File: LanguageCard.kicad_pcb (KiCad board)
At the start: 2 copper layers, 100 x 77.5 mm, 31 parts, among them J1 Apple II Expansion Bus, U1 74LS86, U10 74LS06, U2 74LS08, U3 74LS175, U4 74LS32, U5 74LS08, U6 74LS08, U7 ROM F8 (2716), U8 6264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

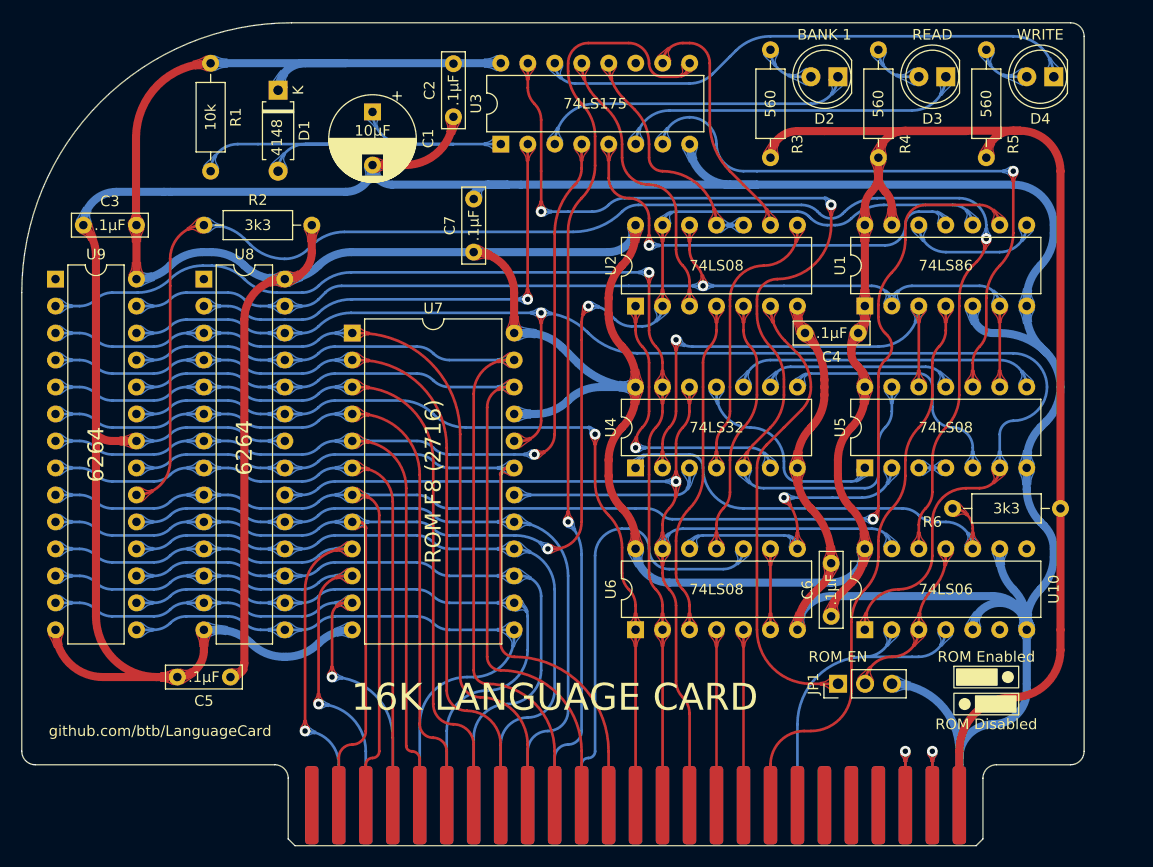
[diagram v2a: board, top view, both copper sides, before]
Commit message: update to Kicad 7
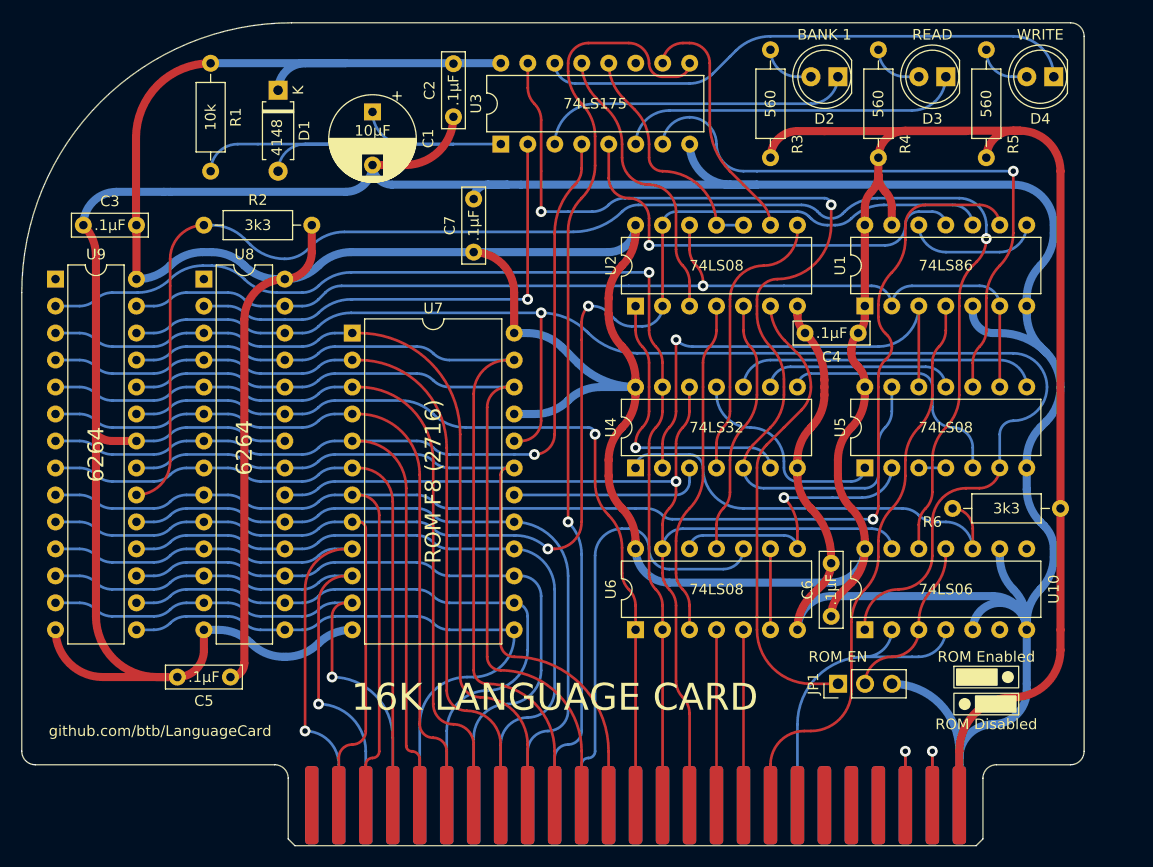
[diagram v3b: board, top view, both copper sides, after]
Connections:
- net /~{R/W} renamed /~{R}/W

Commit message: Larger ROM, enable switch
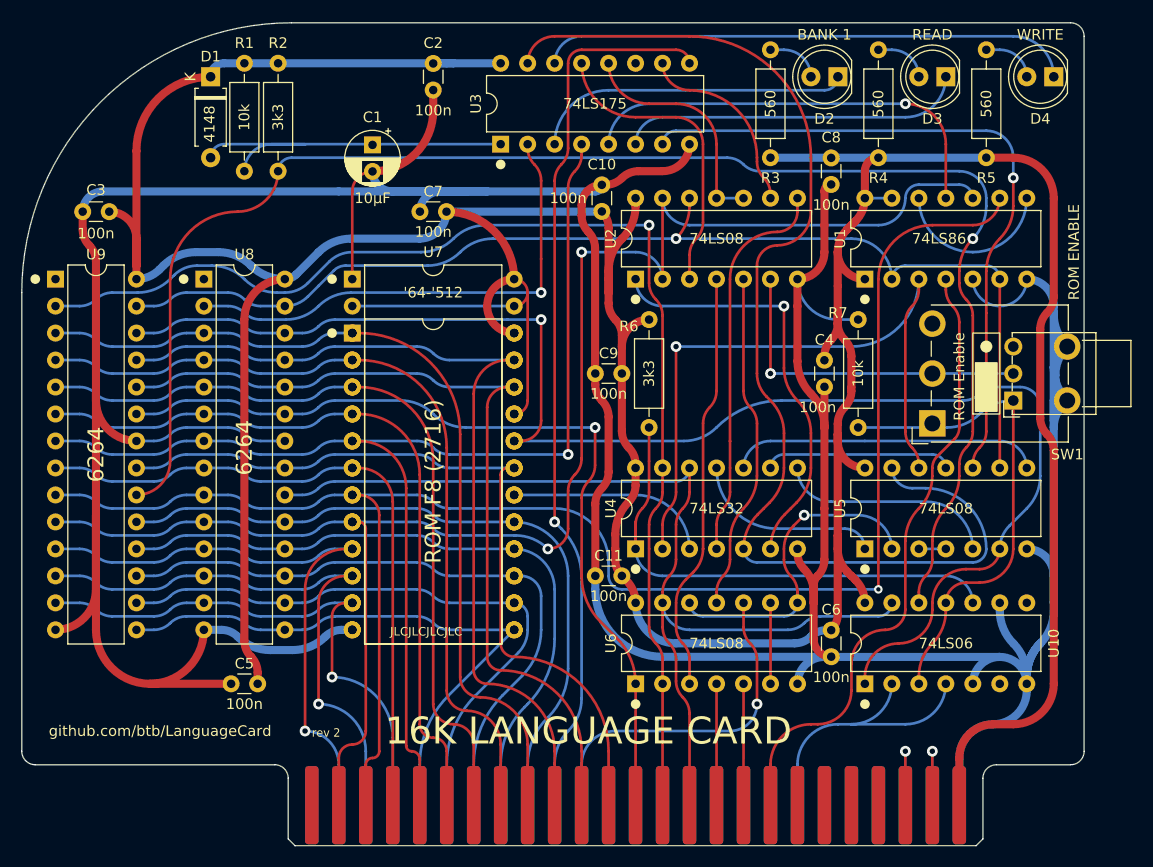
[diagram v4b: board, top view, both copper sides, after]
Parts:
- removed JP1: ROM EN, Connector_PinHeader_2.54mm:PinHeader_1x03_P2.54mm_Vertical
- removed the REF** at (168.9, 89.5)
- removed the REF** at (168.9, 87.0)
- added C10: 100n, Capacitor_THT:C_Disc_D3.0mm_W1.6mm_P2.50mm, F.Cu at (132.7, 43.2)
- added C11: 100n, Capacitor_THT:C_Disc_D3.0mm_W1.6mm_P2.50mm, F.Cu at (134.6, 77.5)
- added C8: 100n, Capacitor_THT:C_Disc_D3.0mm_W1.6mm_P2.50mm, F.Cu at (154.3, 38.1)
- added C9: 100n, Capacitor_THT:C_Disc_D3.0mm_W1.6mm_P2.50mm, F.Cu at (134.6, 58.4)
- added R7: 10k, Resistor_THT:R_Axial_DIN0207_L6.3mm_D2.5mm_P10.16mm_Horizontal, F.Cu at (156.8, 53.3)
- added REF**: ROM Enable, MySymbol:Jumper_SilkScreen, F.Cu at (168.9, 58.4)
- added SW1: ROM ENABLE, MySwitch:SW_Lever_1P2T_Alcoswitch_AE101SD1, F.Cu at (163.8, 58.4)
- added SW1Alt1: ROM ENABLE, Button_Switch_THT:SW_Lever_1P2T_NKK_GW12LxH, F.Cu at (171.4, 61.0)
- added U7Alt1: '64-'512, Package_DIP:DIP-28_W15.24mm, F.Cu at (109.2, 49.5)
- C1: footprint Capacitor_THT:CP_Radial_D8.0mm_P5.00mm -> Capacitor_THT:CP_Radial_D5.0mm_P2.50mm
- C2, C3, C4, C5, C6, C7: value .1μF -> 100n; footprint Capacitor_THT:C_Rect_L7.0mm_W2.0mm_P5.00mm -> Capacitor_THT:C_Disc_D3.0mm_W1.6mm_P2.50mm
- moved R6 29.6 mm to (137.2, 63.5), turned to 90 degrees
- moved R2 8.64 mm to (102.2, 39.4), turned to 90 degrees
- moved U5 7.63 mm to (157.5, 74.9)
- moved U4 7.62 mm to (135.9, 74.9)
- moved D1 6.48 mm to (95.9, 30.5)
- moved U6 5.09 mm to (135.9, 87.6)
- moved U10 5.09 mm to (157.5, 87.6)
- moved C7 4.59 mm to (118.1, 43.2), turned to 180 degrees
- moved C4 4.08 mm to (153.7, 57.2), turned to -90 degrees
- moved R1 3.17 mm to (99.1, 29.2)
- moved C2 3.16 mm to (116.8, 31.7)
- moved C1 3.10 mm to (111.1, 36.9)
- moved C5 2.64 mm to (100.3, 87.6)
- moved U2 2.54 mm to (135.9, 49.5)
- moved U1 2.53 mm to (157.5, 49.5)
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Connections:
- net Net-(U7-~{CE}/PGM) renamed /~{RCE}
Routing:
- net GND: track 377.1 -> 469.8 mm
- net /ROM: track 16.0 -> 46.8 mm
- net +5V: track 409.5 -> 430.6 mm
- net /~{R}/W: track 45.1 -> 64.0 mm
- net /WE: track 95.6 -> 112.6 mm, vias 2 -> 0
- net /~{RESET}: track 48.1 -> 35.1 mm
- net Net-(U2-Pad1): track 27.7 -> 39.9 mm
- net /ROMCE: track 43.8 -> 31.7 mm, vias 0 -> 1
- net Net-(U2-Pad8): track 26.5 -> 36.7 mm
- net /BR/W: track 99.2 -> 109.2 mm
- net /A1: track 150.4 -> 159.9 mm
- net /PHI0: track 42.5 -> 33.2 mm, vias 0 -> 1
- net /~{A13}: track 139.0 -> 146.9 mm
- net Net-(U2-Pad4): track 31.7 -> 39.5 mm
- net Net-(U2-Pad5): track 24.1 -> 31.8 mm
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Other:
- board text added: "JLCJLCJLCJLC"
- board text added: "rev ${REVISION}"

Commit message: dual rom config, lots of tweaks
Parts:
- removed SW1Alt1: ROM ENABLE, Button_Switch_THT:SW_Lever_1P2T_NKK_GW12LxH
- added JP1: ROM Enable, Connector_PinHeader_2.54mm:PinHeader_2x03_P2.54mm_Vertical, F.Cu at (170.8, 61.0)
- added JP2: DUAL ROM, Jumper:SolderJumper-2_P1.3mm_Open_RoundedPad1.0x1.5mm, B.Cu at (173.4, 58.4)
- added JP3: SPST, Jumper:SolderJumper-2_P1.3mm_Open_RoundedPad1.0x1.5mm, B.Cu at (170.8, 57.1)
- added R8: 10k, Resistor_THT:R_Axial_DIN0207_L6.3mm_D2.5mm_P10.16mm_Horizontal, F.Cu at (141.0, 63.5)
- added REF**: ROM Disabled, MySymbol:Jumper_SilkScreen, F.Cu at (218.4, 82.5)
- added REF**: Upper ROM Enabled, MySymbol:Jumper_SilkScreen, F.Cu at (231.1, 95.2)
- added REF**: Lower ROM Enabled, MySymbol:Jumper_SilkScreen, F.Cu at (241.3, 95.2)
- added REF**: ROM Disabled, MySymbol:Jumper_SilkScreen, F.Cu at (218.4, 95.2)
- REF**: value ROM Enable -> 2K ROM Enabled
- SW1: footprint MySwitch:SW_Lever_1P2T_Alcoswitch_AE101SD1 -> MySwitch:SW_Lever_2P2T_Alcoswitch_AE203SD1
- U7: value ROM F8 (2716) -> ROM F8 (2716/32)
- moved REF** 66.7 mm to (231.1, 82.5)
- moved C10 43.3 mm to (175.9, 40.6)
- moved C7 21.6 mm to (133.3, 58.4)
- moved C9 15.5 mm to (132.1, 43.2), turned to 90 degrees
- moved C3 8.61 mm to (92.1, 40.7), turned to -90 degrees
- moved C5 8.26 mm to (92.1, 88.2), turned to 90 degrees
- moved R7 8.25 mm to (148.6, 53.3)
- moved C6 5.26 mm to (155.6, 77.5), turned to 180 degrees
- moved R2 4.62 mm to (106.7, 38.1)
- moved D1 4.62 mm to (100.3, 29.2)
- moved R1 4.62 mm to (103.5, 27.9)
- moved C4 2.26 mm to (155.6, 58.4), turned to 180 degrees
- moved C1 1.42 mm to (111.8, 35.6)
- moved C8 1.27 mm to (154.3, 39.4)
- moved R3 1.27 mm to (148.6, 29.2)
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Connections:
- net /~{RCE} renamed /~{ROMCE}
- R7 pad 2: /ROM -> /ROMEN
- SW1 pad 1: /ROM -> unconnected-(SW1A-A-Pad1)
- SW1 pad 2: /ROMCE -> /ROMA11/VPP/~{WE}
- SW1 pad 3: (no net) -> GND
- U10 pad 11: /ROM -> /ROMEN
- U10 pad 3: /ROM -> /ROMEN
- U2 pad 6: /ROMCE -> /F8SEL
- U7 pad 21: +5V -> /ROMA11/VPP/~{WE}
- U7Alt1 pad 23: +5V -> /ROMA11/VPP/~{WE}
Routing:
- net GND: track 469.8 -> 19.7 mm
- net +5V: track 430.6 -> 4.45 mm
- net /ROMEN: track 0.00 -> 60.9 mm
- net /ROMA11/VPP/~{WE}: track 0.00 -> 56.3 mm
- net /ROM: track 46.8 -> 0.00 mm
- net /F8SEL: track 0.00 -> 36.0 mm, vias 0 -> 1
- net /ROMCE: track 31.7 -> 0.00 mm, vias 1 -> 0
- net /ROMEN2: track 0.00 -> 11.7 mm
- net /RAMCE: track 138.5 -> 129.6 mm
- net /~{R}/W: track 64.0 -> 72.5 mm
- net /~{RESET}: track 35.1 -> 28.2 mm
- net /~{A13}: track 146.9 -> 153.7 mm
- net Net-(R6-Pad1): track 48.7 -> 54.2 mm
- net /A1: track 159.9 -> 165.2 mm
- net /RAMEN: track 65.2 -> 69.4 mm
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- added copper zone on F.Cu, net +5V
- added copper zone on B.Cu, net GND
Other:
- board text added: "JP1: If not using switch. (front view) 2K ROM: (JP2 open) >2K ROM: (JP2 short)"
- board text added: "JP2: Short, and install DPDT switch (or use pair of jumpers on JP1) for ability to select two different F8 ROM images on a single (larger than 2K) ROM."
- board text added: "JP3: Short if using an SPST switch that only connects outer two pins"
- board text added: "SW1: Toggle switch. Miniature, Sub-miniature, or Ultra- miniature, right angle, SPDT. (Sub, Ultra-mini use JP1 pads) For SPST, short JP3. To switch between two different F8 ROM images on a single 4K or greater chip, short JP2 and use DPDT - must have center OFF (ON-OFF-ON) in order to disable."
- board text added: "U7: Optional. 2K or larger (E)EPROM for overriding the logic board's F8 ROM. Enable using SW1 or JP1."
